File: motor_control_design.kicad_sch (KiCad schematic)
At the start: 78 parts, among them J10 3V3, J2 SWD, J3 VBAT, J4 GND, J5 FC_M/P, J6 Conn_01x06, J8 Conn_01x06, J9 GND, Q1 RF1S9540SM, Q10 2N7002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

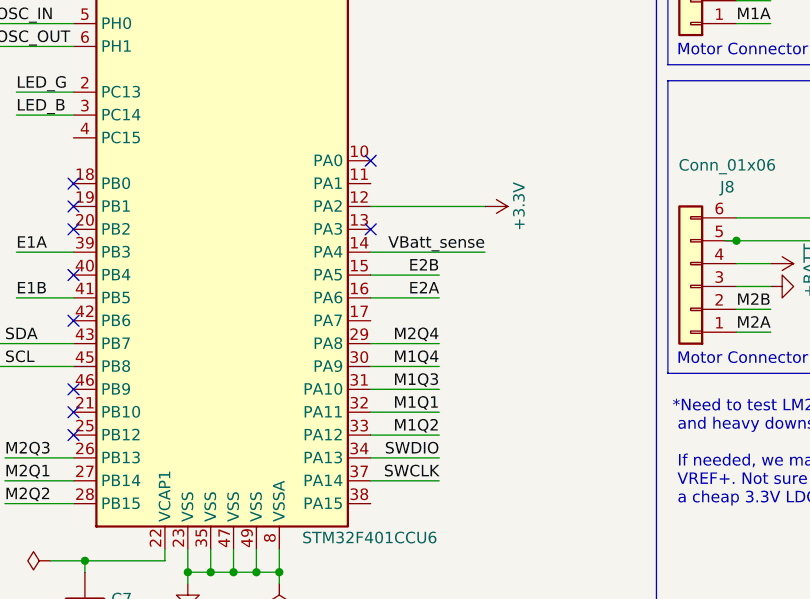
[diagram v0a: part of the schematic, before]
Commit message: Moved M1Q2 and E2B
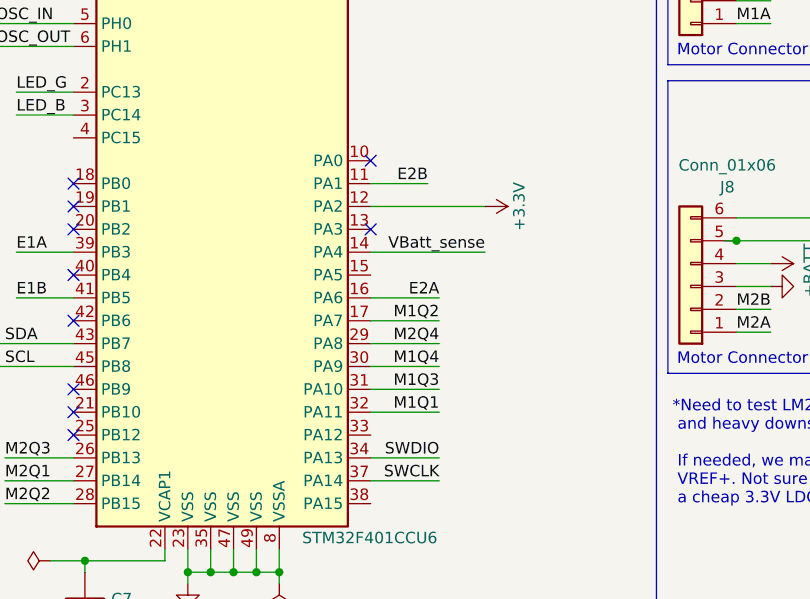
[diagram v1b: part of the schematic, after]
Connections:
- net E2B: now also U1.11 (PA1); no longer U1.15 (PA5)
- net M1Q2: now also U1.17 (PA7); no longer U1.33 (PA12)
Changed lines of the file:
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@@
 	(wire
 		(pts
+			(xy 100.33 95.25) (xy 107.95 95.25)
+		)
+		(stroke
+			(width 0)
+			(type default)
+		)
+	)
+	(wire
+		(pts
 			(xy 59.69 148.59) (xy 63.5 148.59)
 		)
@@
 	(wire
 		(pts
+			(xy 100.33 80.01) (xy 106.68 80.01)
+		)
+		(stroke
+			(width 0)
+			(type default)
+		)
+	)
+	(wire
+		(pts
 			(xy 124.46 160.02) (xy 130.81 160.02)
 		)
@@
 	(wire
 		(pts
-			(xy 100.33 107.95) (xy 107.95 107.95)
-		)
-		(stroke
-			(width 0)
-			(type default)
-		)
-	)
-	(wire
-		(pts
 			(xy 210.82 96.52) (xy 213.36 96.52)
 		)
@@
 	(wire
 		(pts
-			(xy 100.33 90.17) (xy 107.95 90.17)
-		)
-		(stroke
-			(width 0)
-			(type default)
-		)
-	)
-	(wire
-		(pts
 			(xy 168.91 153.67) (xy 167.64 153.67)
 		)
@@
 	)
 	(label "E2B"
-		(at 107.95 90.17 180)
+		(at 106.68 80.01 180)
 		(fields_autoplaced yes)
 		(effects
@@
 	)
 	(label "M1Q2"
-		(at 107.95 107.95 180)
+		(at 107.95 95.25 180)
 		(fields_autoplaced yes)
 		(effects

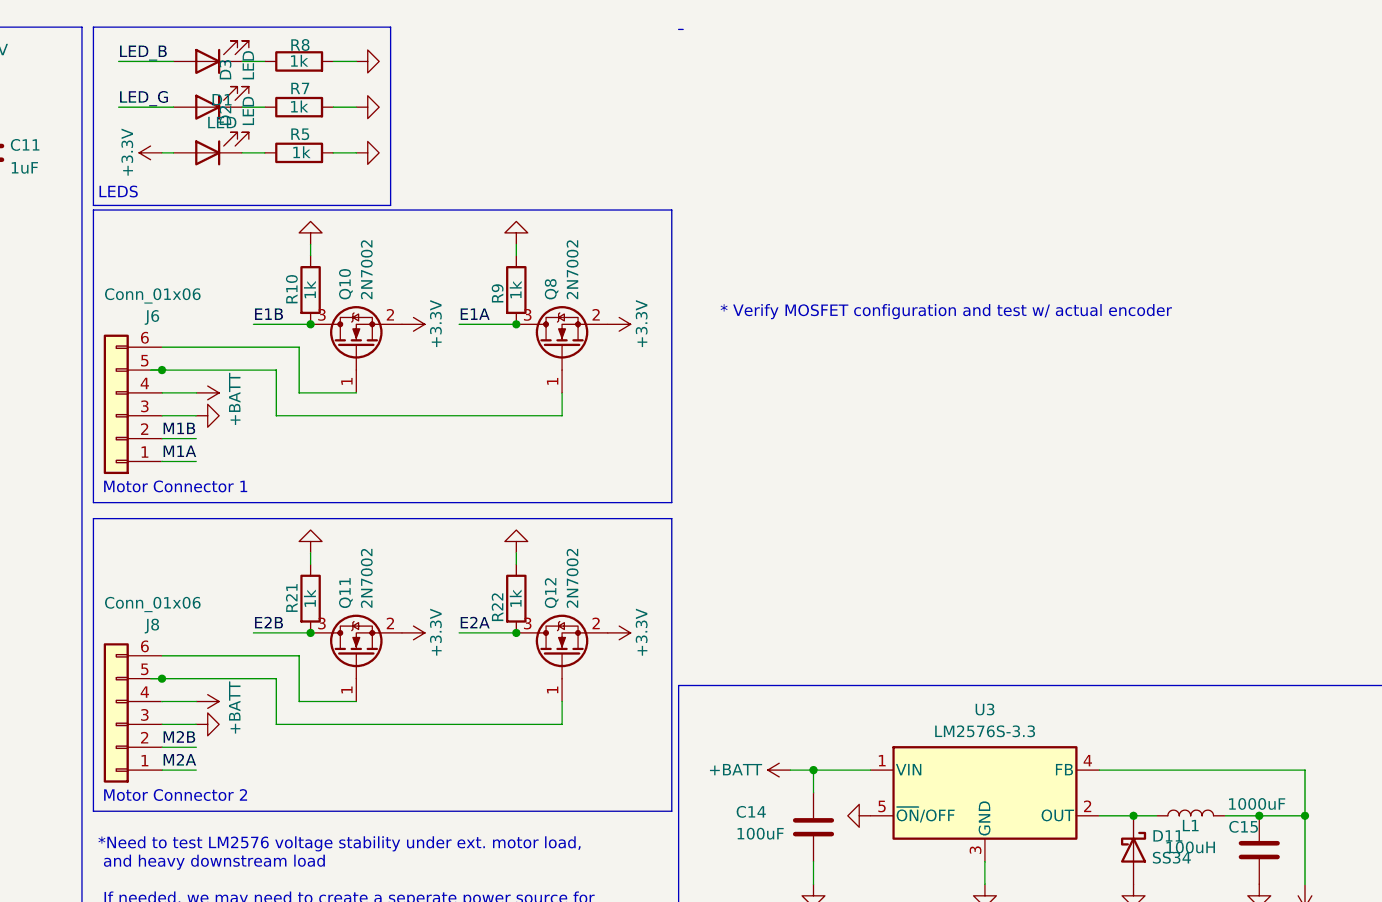
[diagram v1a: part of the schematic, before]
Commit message: 8v power to encoder schematic
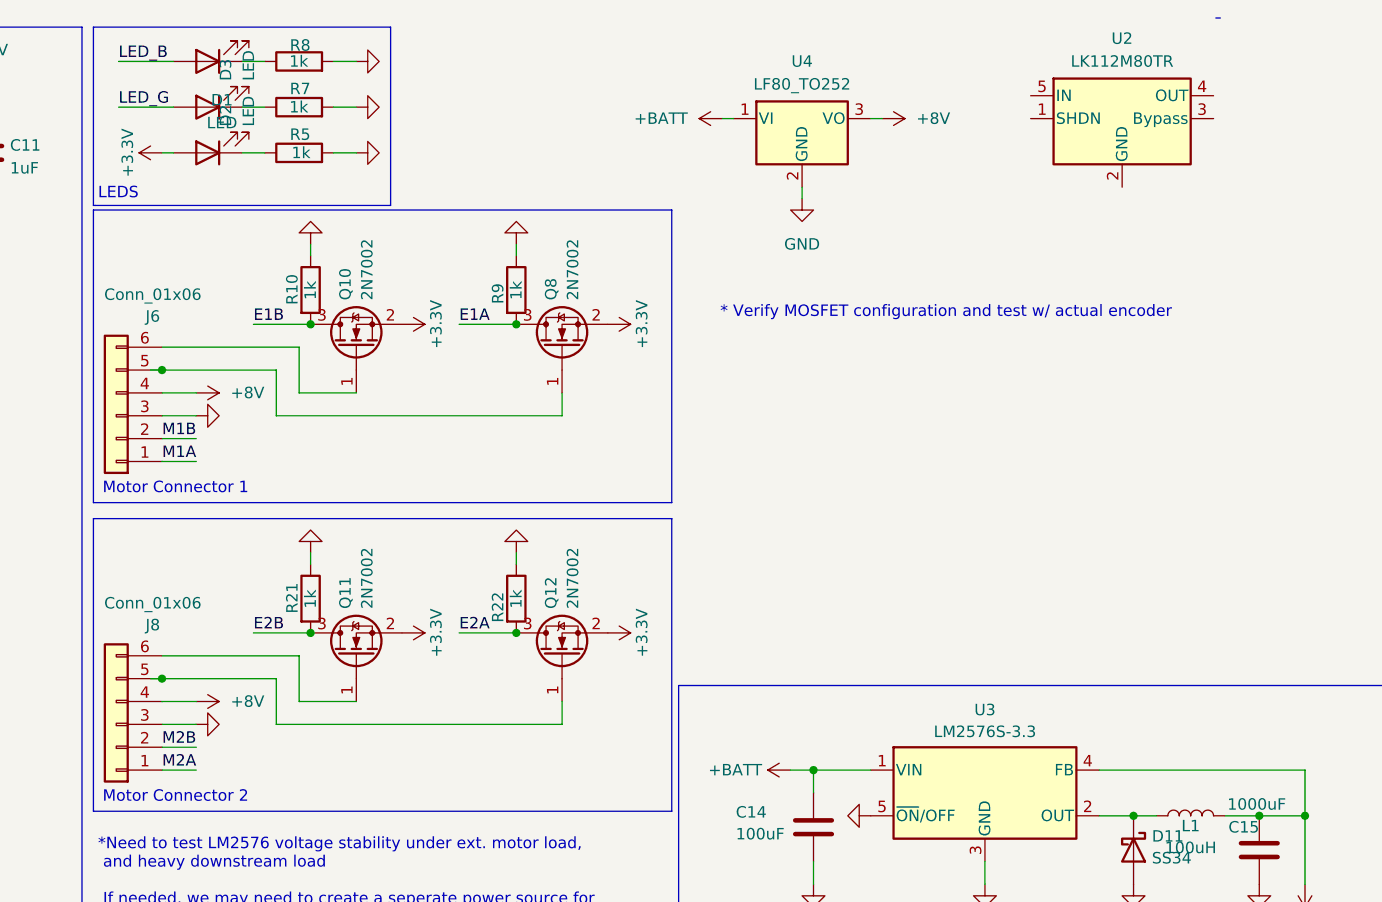
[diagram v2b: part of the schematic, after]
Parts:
- added U2: LK112M80TR, Package_TO_SOT_SMD:SOT-23-5, symbol Regulator_Linear:LK112M80TR
- added U4: LF80_TO252, Package_TO_SOT_SMD:TO-252-2, symbol Regulator_Linear:LF80_TO252
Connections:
- net +BATT: now also U4.1 (VI); no longer J6.4 (Pin_4), J8.4 (Pin_4)
- net GND: now also U4.2 (GND)
- new net +8V: J6.4 (Pin_4), J8.4 (Pin_4), U4.3 (VO)

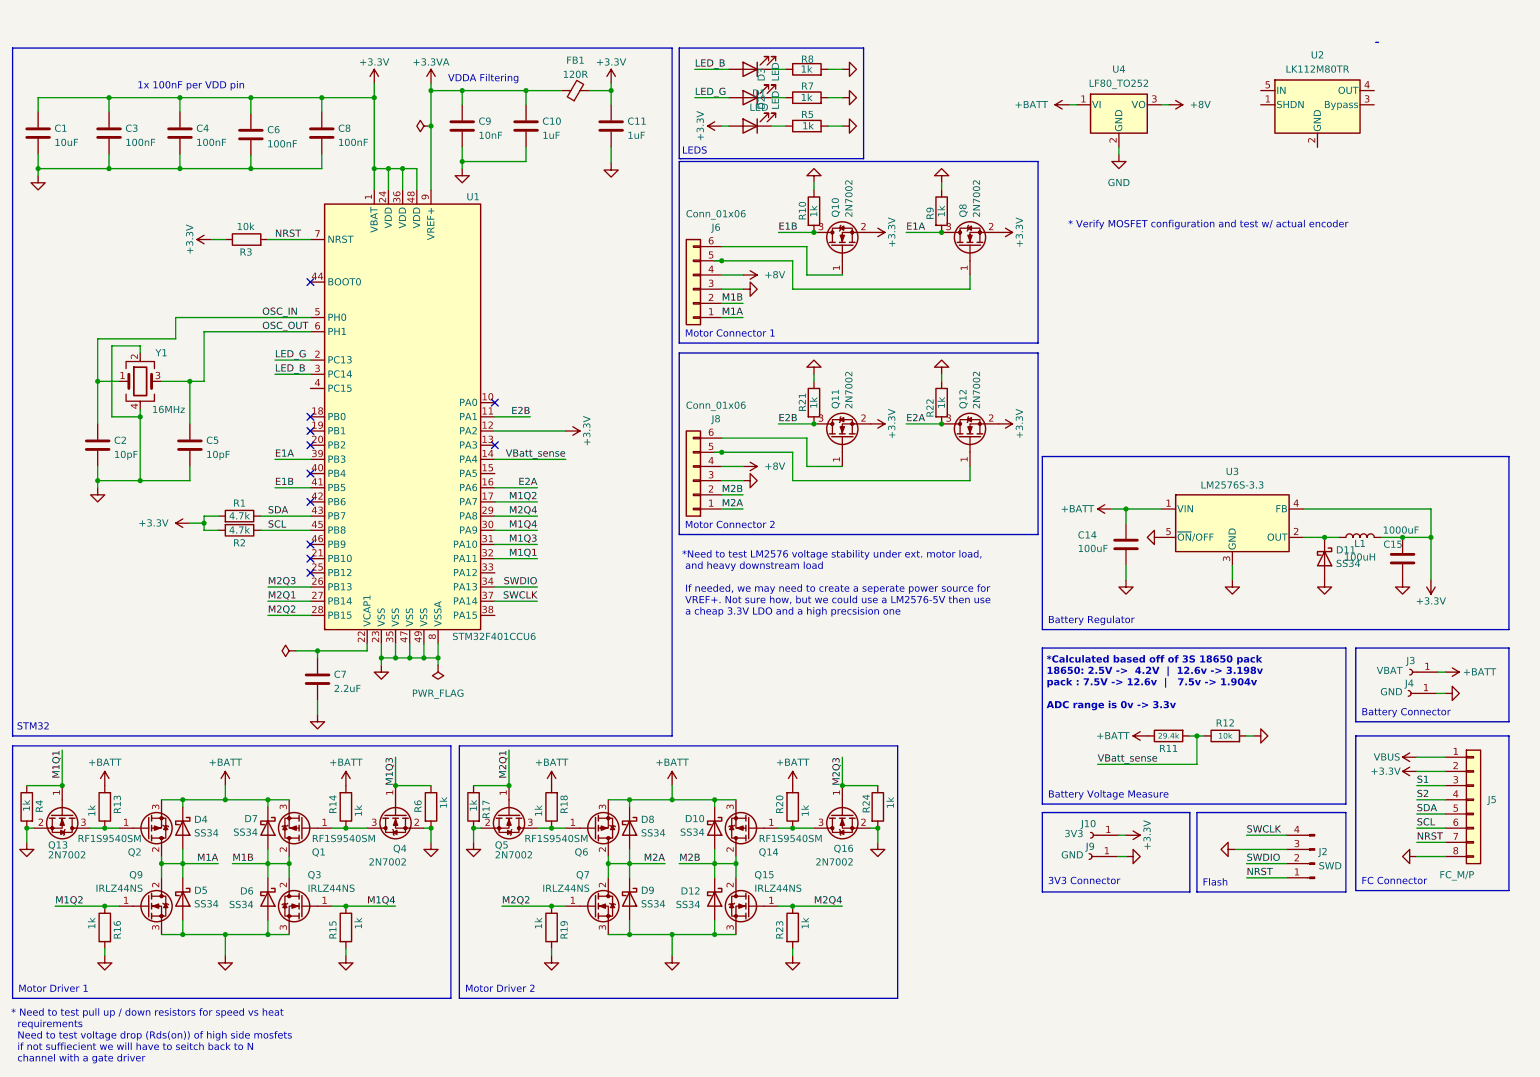
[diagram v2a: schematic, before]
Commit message: USBC schematic started, M1Q1 moved to PA5
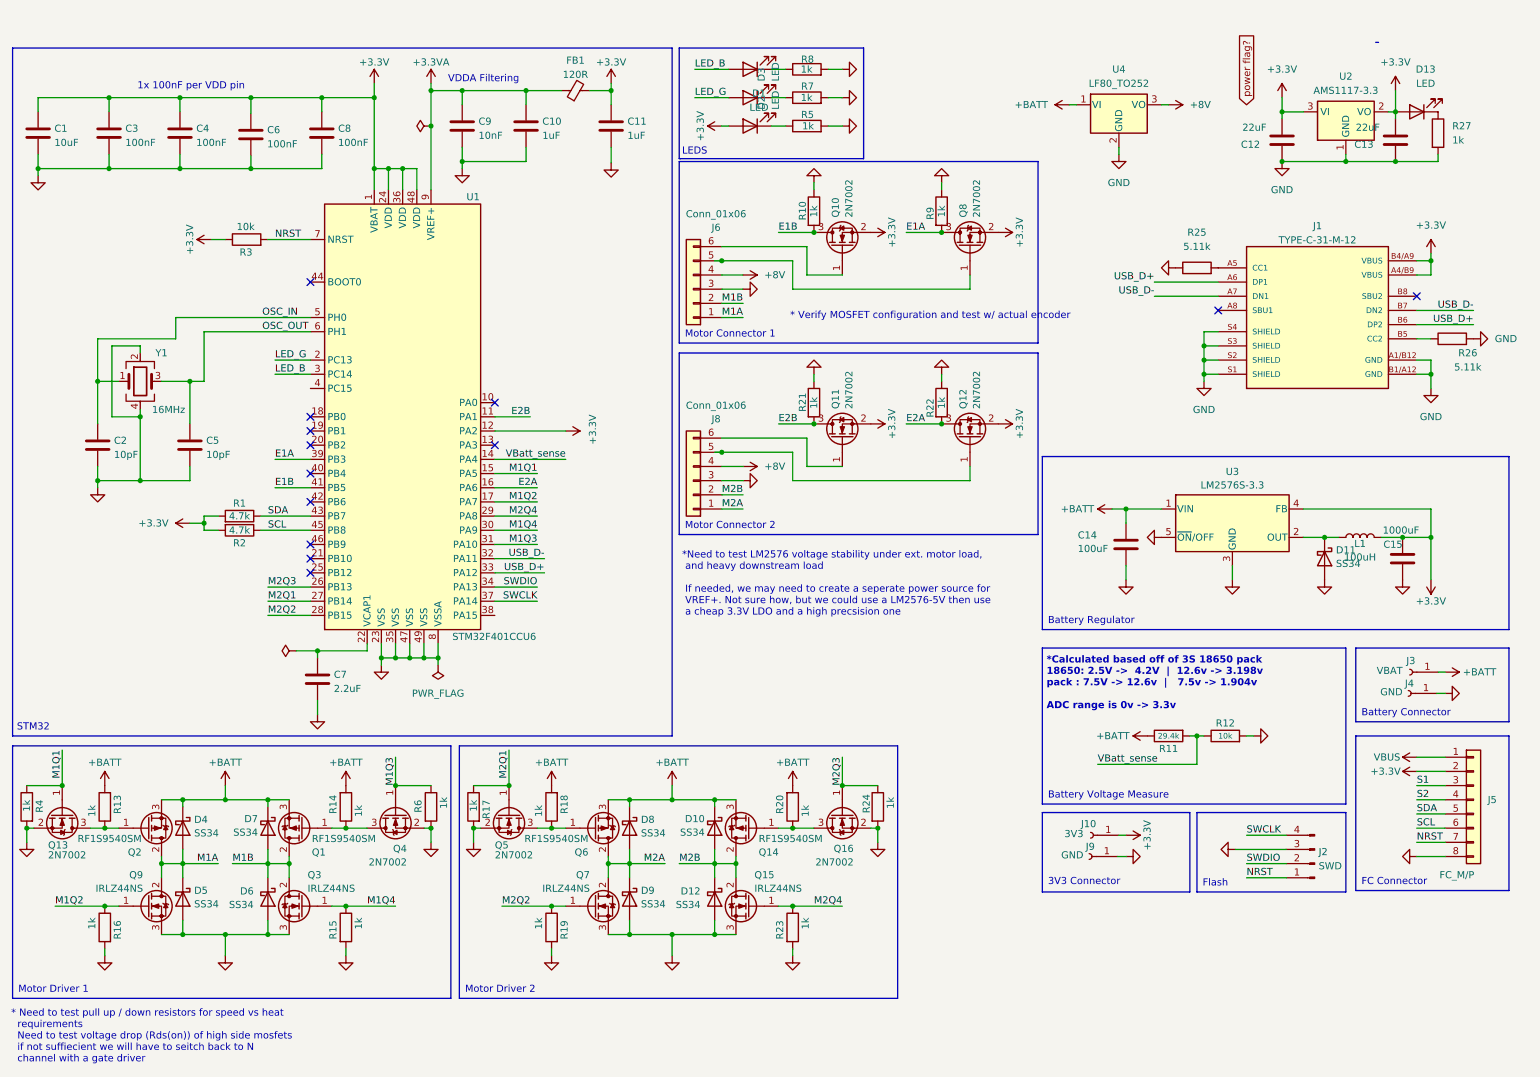
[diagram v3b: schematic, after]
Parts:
- removed U2: LK112M80TR, Package_TO_SOT_SMD:SOT-23-5, symbol Regulator_Linear:LK112M80TR
- added C12, C13: 22uF, symbol Device:C
- added D13: LED, symbol Device:LED
- added J1: TYPE-C-31-M-12, USBC:HRO_TYPE-C-31-M-12, symbol TYPE-C-31-M-12:TYPE-C-31-M-12
- added R25, R26: 5.11k, symbol Device:R
- added R27: 1k, symbol Device:R
- added U2: AMS1117-3.3, Package_TO_SOT_SMD:SOT-223-3_TabPin2, symbol Regulator_Linear:AMS1117-3.3
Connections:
- net +3.3V: now also C12.1, C13.1, D13.2 (A), J1.A4/B9 (VBUS), J1.B4/A9 (VBUS), U2.2 (VO), U2.3 (VI)
- net GND: now also C12.2, C13.2, J1.A1/B12 (GND), J1.B1/A12 (GND), J1.S1 (SHIELD), J1.S2 (SHIELD), J1.S3 (SHIELD), J1.S4 (SHIELD), R25.1, R26.2, R27.2, U2.1 (GND)
- net M1Q1: now also U1.15 (PA5); no longer U1.32 (PA11)
- net USB_D+: now reaches U1.33 (PA12)
- net USB_D+: now also J1.A6 (DP1), J1.B6 (DP2)
- new net: J1.B5 (CC2), R26.1
- new net: D13.1 (K), R27.1
- new net: J1.A5 (CC1), R25.2
- new net USB_D-: J1.A7 (DN1), J1.B7 (DN2), U1.32 (PA11)
- no-connect marks 11 -> 13
